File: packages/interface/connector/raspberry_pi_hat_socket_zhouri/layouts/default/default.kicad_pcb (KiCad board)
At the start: 2 copper layers, 1 part

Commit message: Finish removing net-name overrides from reusable packages
This completes the package-level override cleanup by deleting the remaining
`override_net_name` assignments from the library's reusable package modules and
rebuilding their checked-in layouts so generated net metadata matches source.
The package interfaces stay the same; only the forced net naming was removed so
these modules compose cleanly when imported into downstream designs.

Constraint: The library must stay reusable and avoid imposed internal net names leaking into consuming designs
Constraint: Each changed package must still verify with the repo's Atopile workflow after layout regeneration
Rejected: Stop after the battery frontend cleanup | leaves the same composition hazard in other packages
Rejected: Remove override lines without rebuilding layouts | would leave stale generated PCB net names checked into the repo
Confidence: high
Scope-risk: moderate
Reversibility: clean
Directive: Do not reintroduce `override_net_name` in reusable package modules unless a package is intentionally design-specific
Tested: `uv tool run --from atopile==0.15.4 ato --non-interactive build` in each affected package directory (stm32g0b1kbu6_st, mcp2518fdt_e_sl_microchip, tcan3413ddfr_ti, raspberry_pi_hat_socket_zhouri, tps56637rpar_5v1_5a_ti, tps62933drlr_3v3_ti, bq25756rrvr_4s_2a_ti, tps2121ruxr_20v_4a_ti, tps25730drefr_20v_3a_ti)
Not-tested: Downstream consumer projects that may have been depending on the old forced net names in generated layouts
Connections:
- net +3.3V renamed hv
- net +5V renamed power_5v0-hv
- net GND renamed lv
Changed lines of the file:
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@@
 	(net 38 "P07_GPIO4_GPCLK0")
 	(net 39 "P08_GPIO14_TXD0")
-	(net 41 "+3.3V")
-	(net 42 "GND")
-	(net 43 "+5V")
+	(net 41 "hv")
+	(net 42 "lv")
+	(net 43 "power_5v0-hv")
 	(footprint "ZHOURI_2_54_2_20:HDR-TH_40P-P2.54-V-F-R2-C20-S2.54"
 		(layer "F.Cu")
@@
 			(drill 0.999998)
 			(layers "*.Cu" "*.Mask")
-			(net 42 "GND")
+			(net 42 "lv")
 		)
 		(pad "38" thru_hole circle
@@
 			(drill 0.999998)
 			(layers "*.Cu" "*.Mask")
-			(net 42 "GND")
+			(net 42 "lv")
 		)
 		(pad "33" thru_hole circle
@@
 			(drill 0.999998)
 			(layers "*.Cu" "*.Mask")
-			(net 42 "GND")
+			(net 42 "lv")
 		)
 		(pad "29" thru_hole circle
@@
 			(drill 0.999998)
 			(layers "*.Cu" "*.Mask")
-			(net 42 "GND")
+			(net 42 "lv")
 		)
 		(pad "24" thru_hole circle
@@
 			(drill 0.999998)
 			(layers "*.Cu" "*.Mask")
-			(net 42 "GND")
+			(net 42 "lv")
 		)
 		(pad "19" thru_hole circle
@@
 			(drill 0.999998)
 			(layers "*.Cu" "*.Mask")
-			(net 41 "+3.3V")
+			(net 41 "hv")
 		)
 		(pad "16" thru_hole circle
@@
 			(drill 0.999998)
 			(layers "*.Cu" "*.Mask")
-			(net 42 "GND")
+			(net 42 "lv")
 		)
 		(pad "13" thru_hole circle
@@
 			(drill 0.999998)
 			(layers "*.Cu" "*.Mask")
-			(net 42 "GND")
+			(net 42 "lv")
 		)
 		(pad "8" thru_hole circle
@@
 			(drill 0.999998)
 			(layers "*.Cu" "*.Mask")
-			(net 42 "GND")
+			(net 42 "lv")
 		)
 		(pad "5" thru_hole circle
@@
 			(drill 0.999998)
 			(layers "*.Cu" "*.Mask")
-			(net 43 "+5V")
+			(net 43 "power_5v0-hv")
 		)
 		(pad "3" thru_hole circle
@@
 			(drill 0.999998)
 			(layers "*.Cu" "*.Mask")
-			(net 43 "+5V")
+			(net 43 "power_5v0-hv")
 		)
 		(pad "1" thru_hole rect
@@
 			(drill 0.999998)
 			(layers "*.Cu" "*.Mask")
-			(net 41 "+3.3V")
+			(net 41 "hv")
 		)
 		(embedded_fonts no)

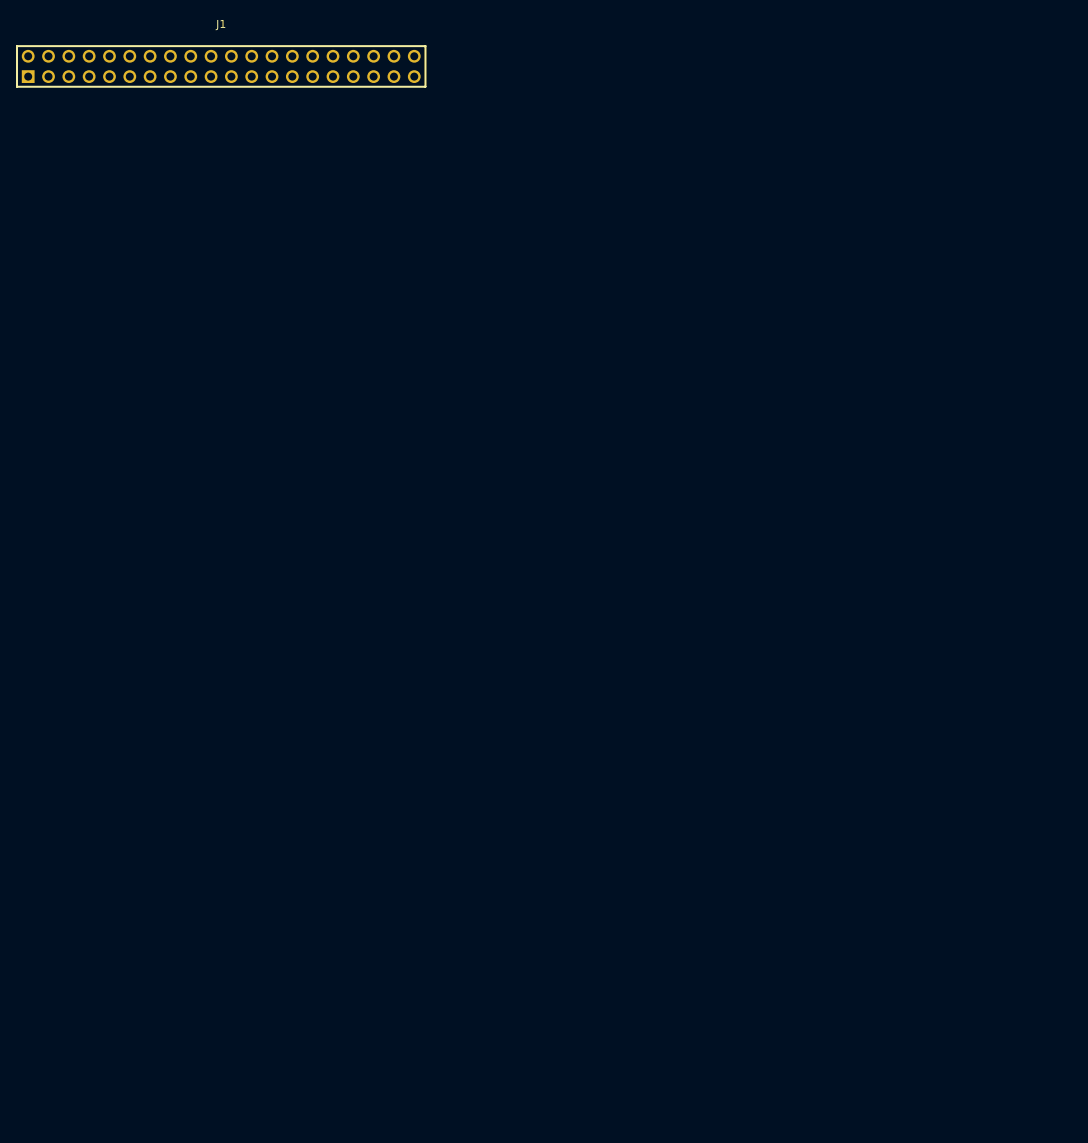
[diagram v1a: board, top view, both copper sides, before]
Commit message: Add Raspberry Pi HAT layout
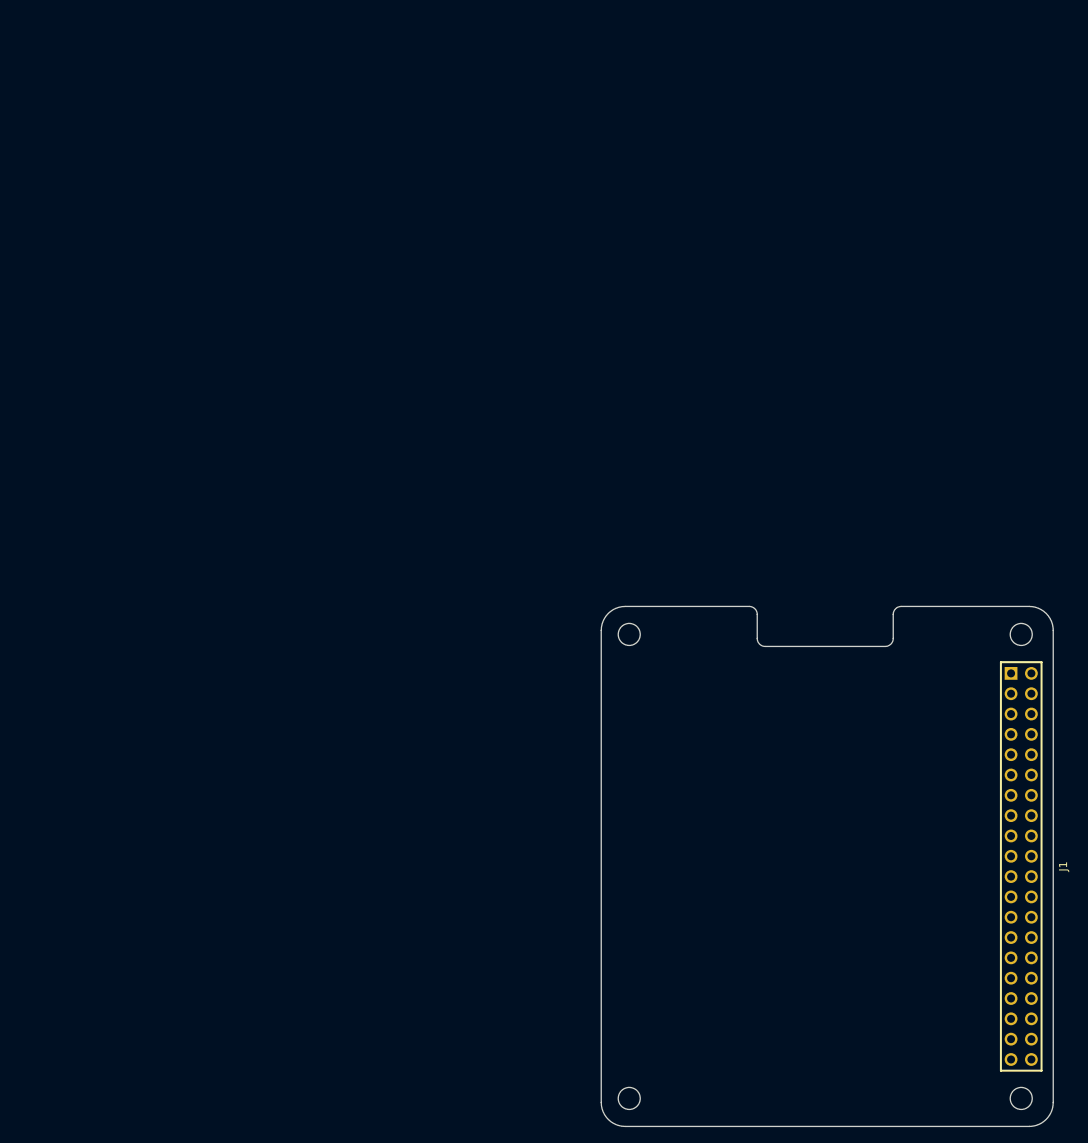
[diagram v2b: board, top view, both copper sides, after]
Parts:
- added H1: , Raspberry_Pi_Hat_Mounting_Hole_NPTH:Raspberry_Pi_Hat_Mounting_Hole_NPTH, F.Cu at (100.0, 71.0)
- added H2: , Raspberry_Pi_Hat_Mounting_Hole_NPTH:Raspberry_Pi_Hat_Mounting_Hole_NPTH, F.Cu at (51.0, 129.0)
- added H3: , Raspberry_Pi_Hat_Mounting_Hole_NPTH:Raspberry_Pi_Hat_Mounting_Hole_NPTH, F.Cu at (51.0, 71.0)
- added H4: , Raspberry_Pi_Hat_Mounting_Hole_NPTH:Raspberry_Pi_Hat_Mounting_Hole_NPTH, F.Cu at (100.0, 129.0)
- moved J1 141.4 mm to (100.0, 100.0), turned to -90 degrees
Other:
- board outline added: 56.5 x 65 mm
